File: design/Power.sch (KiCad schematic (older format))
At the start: 62 parts, among them U2 DRV8302, U3 NCP1117ST33T3G

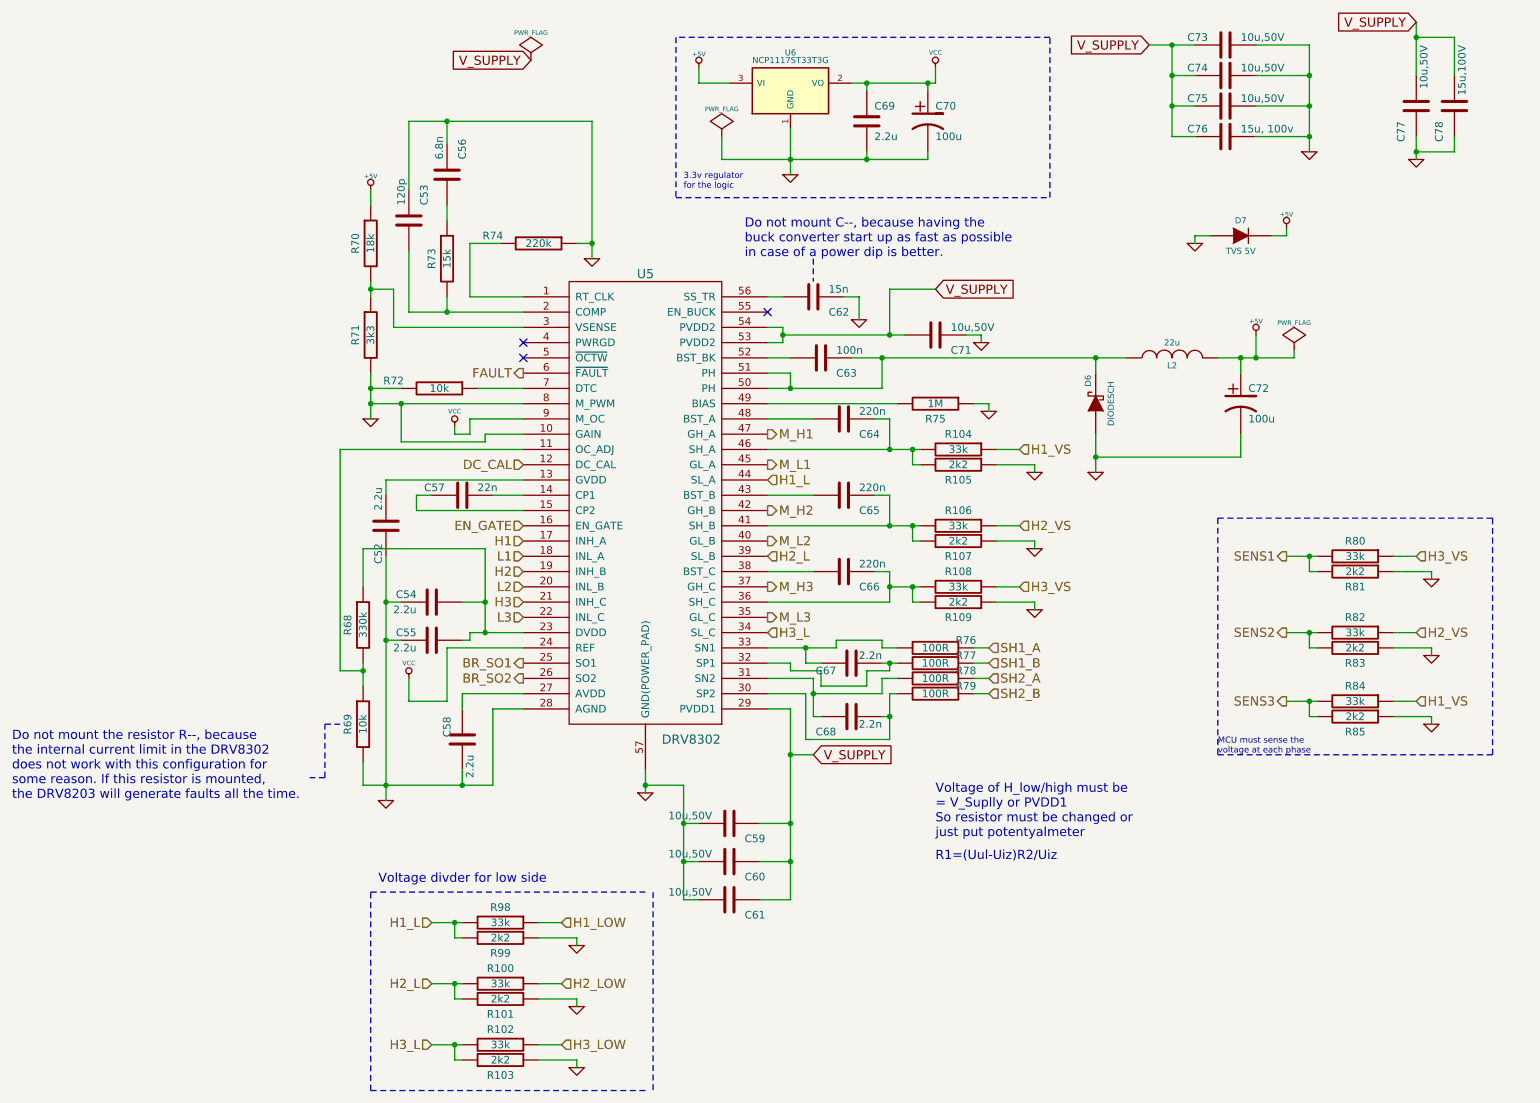
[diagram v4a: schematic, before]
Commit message: Voltage divider for DRV and MCU
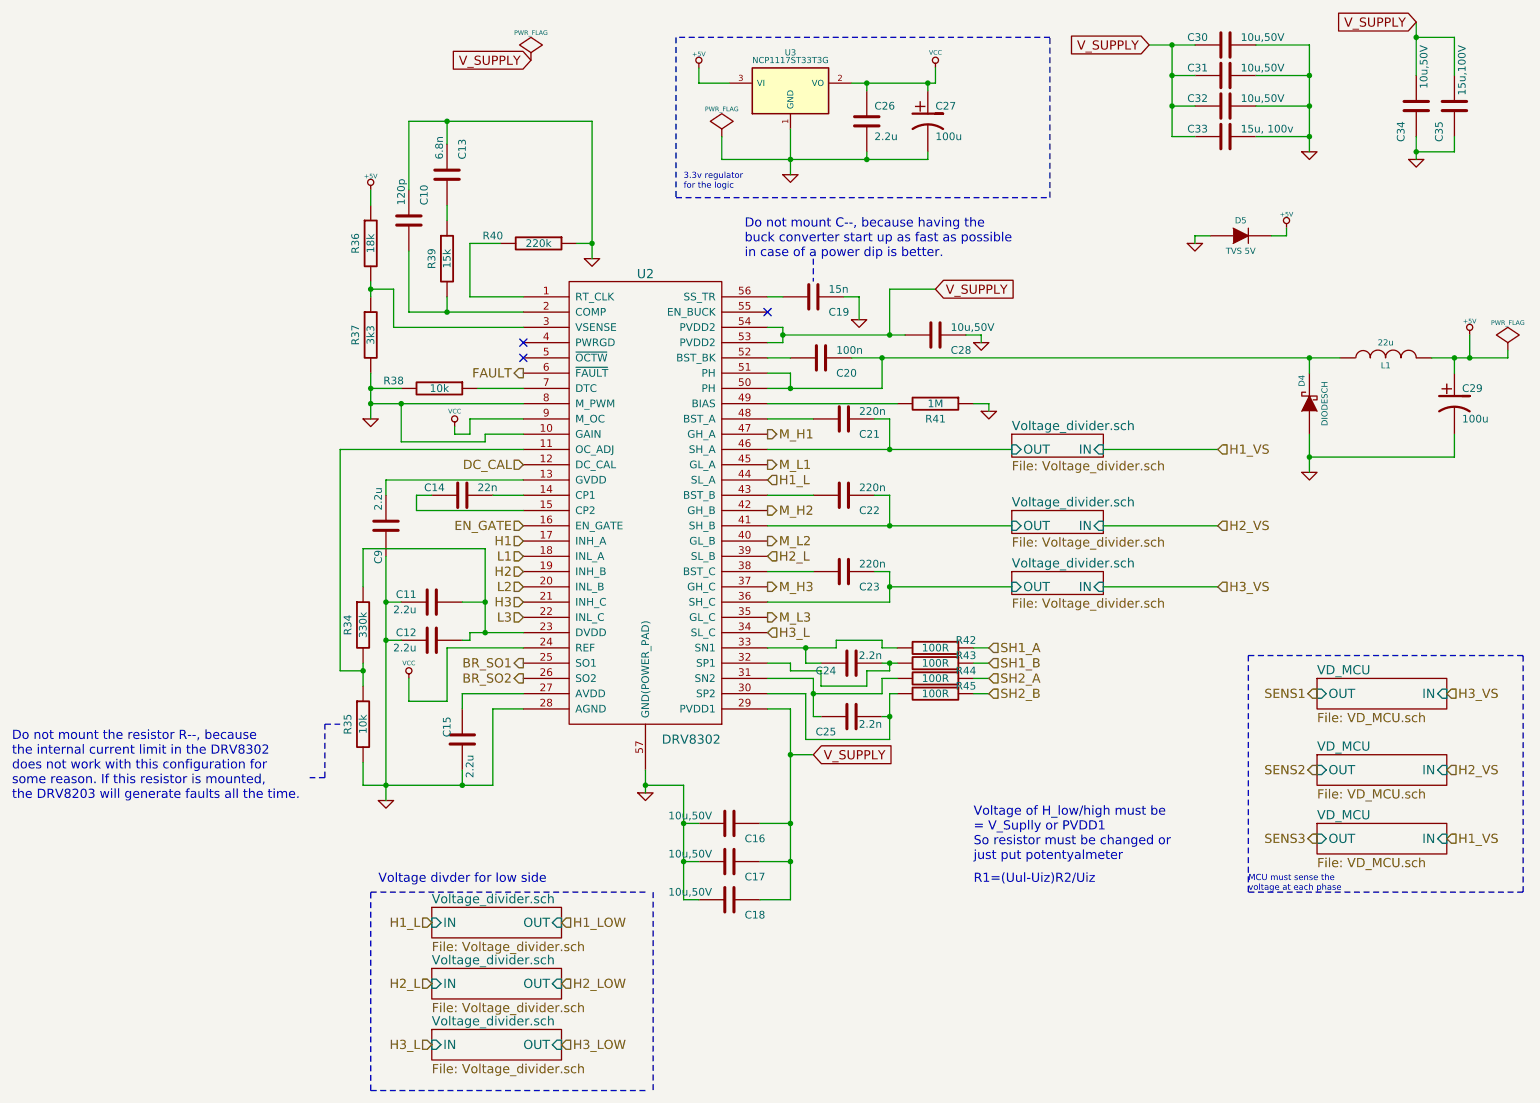
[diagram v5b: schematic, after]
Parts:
- removed R46, R48, R50, R86, R88, R90, R92, R94, R96: 33k, SMD_Packages:SMD-0603_r, symbol R
- removed R47, R49, R51, R87, R89, R91, R93, R95, R97: 2k2, SMD_Packages:SMD-0603_r, symbol R
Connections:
- net Voltage_divider.sch/OUT: now reaches C21.1, U2.46 (SH_A)
- net Voltage_divider.sch/OUT: now reaches C23.1, U2.36 (SH_C)
- net Voltage_divider.sch/OUT: now reaches C22.1, U2.41 (SH_B)
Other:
- moved on the sheet: C29, D4, L1

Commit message: Fix some ERC error, add decoupling cap to Vref+ and make some small changes to lib
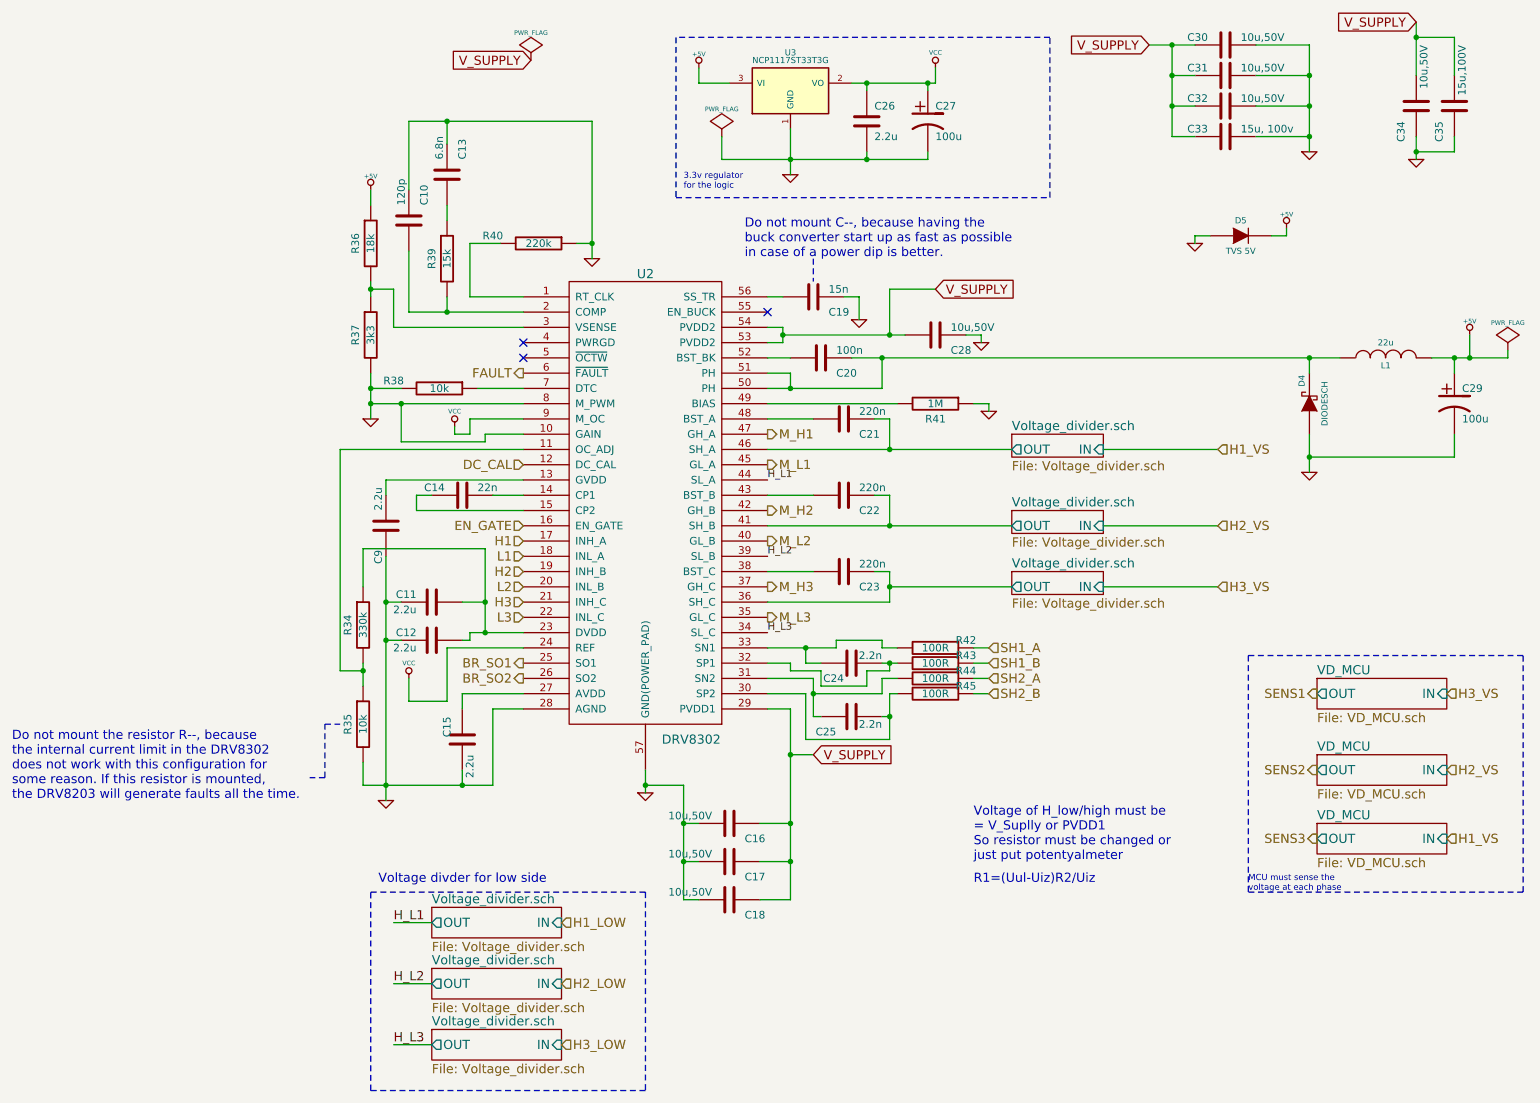
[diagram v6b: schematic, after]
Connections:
- net Voltage_divider.sch/OUT is gone; now on net Voltage_divider.sch/OUT: C22.1, U2.41 (SH_B)
- net Voltage_divider.sch/OUT: no longer C21.1, U2.46 (SH_A)
- net H1_L renamed H_L1
- net H2_L renamed H_L2
- net H3_L renamed H_L3
- new net Voltage_divider.sch/OUT: C21.1, U2.46 (SH_A)

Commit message: PCB
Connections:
- net Voltage_divider.sch/OUT is gone; now on net Voltage_divider.sch/OUT: C22.1, U2.41 (SH_B)
- net Voltage_divider.sch/OUT: no longer C21.1, U2.46 (SH_A)
- new net Voltage_divider.sch/OUT: C21.1, U2.46 (SH_A)
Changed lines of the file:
@@
 AR Path="/504F83BE/504FB755" Ref="#PWR043"  Part="1"
 AR Path="/54B735D5/504FB755" Ref="#PWR079"  Part="1"
-F 0 "#PWR079" H 6750 2700 30  0001 C CNN
+F 0 "#PWR043" H 6750 2700 30  0001 C CNN
 F 1 "GND" H 6750 2630 30  0001 C CNN
 F 2 "" H 6750 2700 60  0001 C CNN
@@
 AR Path="/504F83BE/504FBA7B" Ref="#PWR044"  Part="1"
 AR Path="/54B735D5/504FBA7B" Ref="#PWR080"  Part="1"
-F 0 "#PWR080" H 7600 3300 30  0001 C CNN
+F 0 "#PWR044" H 7600 3300 30  0001 C CNN
 F 1 "GND" H 7600 3230 30  0001 C CNN
 F 2 "" H 7600 3300 60  0001 C CNN
@@
 AR Path="/504F83BE/504FBEC1" Ref="#PWR045"  Part="1"
 AR Path="/54B735D5/504FBEC1" Ref="#PWR081"  Part="1"
-F 0 "#PWR081" H 9700 3700 30  0001 C CNN
+F 0 "#PWR045" H 9700 3700 30  0001 C CNN
 F 1 "GND" H 9700 3630 30  0001 C CNN
 F 2 "" H 9700 3700 60  0001 C CNN
@@
 AR Path="/504F83BE/504FBFA1" Ref="#PWR046"  Part="1"
 AR Path="/54B735D5/504FBFA1" Ref="#PWR082"  Part="1"
-F 0 "#PWR082" H 10750 2890 20  0001 C CNN
+F 0 "#PWR046" H 10750 2890 20  0001 C CNN
 F 1 "+5V" H 10750 2890 30  0000 C CNN
 F 2 "" H 10750 2800 60  0001 C CNN
@@
 AR Path="/504F83BE/504FC2A8" Ref="#PWR047"  Part="1"
 AR Path="/54B735D5/504FC2A8" Ref="#PWR083"  Part="1"
-F 0 "#PWR083" H 3650 5850 30  0001 C CNN
+F 0 "#PWR047" H 3650 5850 30  0001 C CNN
 F 1 "GND" H 3650 5780 30  0001 C CNN
 F 2 "" H 3650 5850 60  0001 C CNN
@@
 AR Path="/504F83BE/504FC918" Ref="#PWR048"  Part="1"
 AR Path="/54B735D5/504FC918" Ref="#PWR084"  Part="1"
-F 0 "#PWR084" H 5350 5800 30  0001 C CNN
+F 0 "#PWR048" H 5350 5800 30  0001 C CNN
 F 1 "GND" H 5350 5730 30  0001 C CNN
 F 2 "" H 5350 5800 60  0001 C CNN
@@
 AR Path="/504F83BE/504FDE04" Ref="#PWR049"  Part="1"
 AR Path="/54B735D5/504FDE04" Ref="#PWR085"  Part="1"
-F 0 "#PWR085" H 3550 3350 30  0001 C CNN
+F 0 "#PWR049" H 3550 3350 30  0001 C CNN
 F 1 "GND" H 3550 3280 30  0001 C CNN
 F 2 "" H 3550 3350 60  0001 C CNN
@@
 AR Path="/504F83BE/504FE598" Ref="#PWR050"  Part="1"
 AR Path="/54B735D5/504FE598" Ref="#PWR086"  Part="1"
-F 0 "#PWR086" H 5000 2300 30  0001 C CNN
+F 0 "#PWR050" H 5000 2300 30  0001 C CNN
 F 1 "GND" H 5000 2230 30  0001 C CNN
 F 2 "" H 5000 2300 60  0001 C CNN
@@
 AR Path="/504F83BE/504FE8CD" Ref="#PWR051"  Part="1"
 AR Path="/54B735D5/504FE8CD" Ref="#PWR087"  Part="1"
-F 0 "#PWR087" H 3550 1940 20  0001 C CNN
+F 0 "#PWR051" H 3550 1940 20  0001 C CNN
 F 1 "+5V" H 3550 1940 30  0000 C CNN
 F 2 "" H 3550 1850 60  0001 C CNN
@@
 AR Path="/504F83BE/50500B40" Ref="#PWR052"  Part="1"
 AR Path="/54B735D5/50500B40" Ref="#PWR088"  Part="1"
-F 0 "#PWR088" H 6300 1750 30  0001 C CNN
+F 0 "#PWR052" H 6300 1750 30  0001 C CNN
 F 1 "GND" H 6300 1680 30  0001 C CNN
 F 2 "" H 6300 1750 60  0001 C CNN
@@
 AR Path="/504F83BE/50500B46" Ref="#PWR053"  Part="1"
 AR Path="/54B735D5/50500B46" Ref="#PWR089"  Part="1"
-F 0 "#PWR089" H 7250 1150 30  0001 C CNN
+F 0 "#PWR053" H 7250 1150 30  0001 C CNN
 F 1 "VCC" H 7250 1150 30  0000 C CNN
 F 2 "" H 7250 1050 60  0001 C CNN
@@
 AR Path="/504F83BE/50500BBC" Ref="#PWR054"  Part="1"
 AR Path="/54B735D5/50500BBC" Ref="#PWR090"  Part="1"
-F 0 "#PWR090" H 5700 1140 20  0001 C CNN
+F 0 "#PWR054" H 5700 1140 20  0001 C CNN
 F 1 "+5V" H 5700 1140 30  0000 C CNN
 F 2 "" H 5700 1050 60  0001 C CNN
@@
 AR Path="/504F83BE/505014BC" Ref="#PWR055"  Part="1"
 AR Path="/54B735D5/505014BC" Ref="#PWR091"  Part="1"
-F 0 "#PWR091" H 3800 5150 30  0001 C CNN
+F 0 "#PWR055" H 3800 5150 30  0001 C CNN
 F 1 "VCC" H 3800 5150 30  0000 C CNN
 F 2 "" H 3800 5050 60  0001 C CNN
@@
 AR Path="/504F83BE/50510100" Ref="#FLG056"  Part="1"
 AR Path="/54B735D5/50510100" Ref="#FLG092"  Part="1"
-F 0 "#FLG092" H 11000 2995 30  0001 C CNN
+F 0 "#FLG056" H 11000 2995 30  0001 C CNN
 F 1 "PWR_FLAG" H 11000 3080 30  0000 C CNN
 F 2 "" H 11000 2900 60  0001 C CNN
@@
 AR Path="/504F83BE/505104A0" Ref="#FLG057"  Part="1"
 AR Path="/54B735D5/505104A0" Ref="#FLG093"  Part="1"
-F 0 "#FLG093" H 5850 1595 30  0001 C CNN
+F 0 "#FLG057" H 5850 1595 30  0001 C CNN
 F 1 "PWR_FLAG" H 5850 1680 30  0000 C CNN
 F 2 "" H 5850 1500 60  0001 C CNN
@@
 AR Path="/504F83BE/505105A5" Ref="#FLG058"  Part="1"
 AR Path="/54B735D5/505105A5" Ref="#FLG094"  Part="1"
-F 0 "#FLG094" H 4600 1095 30  0001 C CNN
+F 0 "#FLG058" H 4600 1095 30  0001 C CNN
 F 1 "PWR_FLAG" H 4600 1180 30  0000 C CNN
 F 2 "" H 4600 1000 60  0001 C CNN
@@
 AR Path="/504F83BE/5051337C" Ref="#PWR059"  Part="1"
 AR Path="/54B735D5/5051337C" Ref="#PWR095"  Part="1"
-F 0 "#PWR095" H 7550 2850 30  0001 C CNN
+F 0 "#PWR059" H 7550 2850 30  0001 C CNN
 F 1 "GND" H 7550 2780 30  0001 C CNN
 F 2 "" H 7550 2850 60  0001 C CNN
@@
 AR Path="/504F83BE/5058357A" Ref="#PWR060"  Part="1"
 AR Path="/54B735D5/5058357A" Ref="#PWR096"  Part="1"
-F 0 "#PWR096" H 4100 3500 30  0001 C CNN
+F 0 "#PWR060" H 4100 3500 30  0001 C CNN
 F 1 "VCC" H 4100 3500 30  0000 C CNN
 F 2 "" H 4100 3400 60  0001 C CNN
@@
 AR Path="/504F83BE/510944D0" Ref="#PWR061"  Part="1"
 AR Path="/54B735D5/510944D0" Ref="#PWR097"  Part="1"
-F 0 "#PWR097" H 9700 1600 30  0001 C CNN
+F 0 "#PWR061" H 9700 1600 30  0001 C CNN
 F 1 "GND" H 9700 1530 30  0001 C CNN
 F 2 "" H 9700 1600 60  0001 C CNN
@@
 0D 0D 85 50 5B 08 A1 71 E3 C6 45 47 47 77 AB F8 CD C0 F0 65 C3 18 9A 0F 4F 4B 4B 4B 51 51 51 53
 53 93 40 20 30 31 31 61 94 40 19 18 18 43 C3 C0 C0 A0 72 FE 07 CF 64 8C 61 E1 12 74 DD 00 00 00
-00 49 45 4E 44 AE 42 60 82 14
+00 49 45 4E 44 AE 42 60 82 D9
 EndData
 $EndBitmap
@@
 20 10 88 31 C3 77 F3 62 81 40 20 10 08 04 02 81 E0 1F 14 E4 21 10 08 04 02 81 40 8C 41 50 90 87
 40 20 10 08 04 02 31 06 41 41 1E 02 81 40 20 10 08 C4 18 E4 FF 01 14 B1 03 90 4A B9 68 69 00 00
-00 00 49 45 4E 44 AE 42 60 82 83
+00 00 49 45 4E 44 AE 42 60 82 21
 EndData
 $EndBitmap
@@
 A1 C7 18 00 00 C0 28 C8 B2 00 00 00 46 41 96 05 00 00 30 0A B2 2C 00 00 80 51 90 65 01 00 00 8C
 82 2C 0B 00 00 60 14 64 59 00 00 00 A3 FC 7F BD 9B 69 A6 C1 67 F0 EA 00 00 00 00 49 45 4E 44 AE
-42 60 82 0B
+42 60 82 09
 EndData
 $EndBitmap
@@
 AB D8 39 0B 59 91 9E DF A8 2A 5B EE 54 3A FD 71 ED 71 2F 29 C3 82 EC 80 87 06 6E C3 98 10 30 3B
 62 9A BB 2D 03 B8 C4 64 FC B5 26 AC 13 9B D1 39 40 41 C1 D6 78 4C 84 BF 94 F0 6F E1 BF 96 F0 0F
-FF 77 E2 FF 1F 0F 43 55 32 21 1C 08 16 00 00 00 00 49 45 4E 44 AE 42 60 82 7C
+FF 77 E2 FF 1F 0F 43 55 32 21 1C 08 16 00 00 00 00 49 45 4E 44 AE 42 60 82 54
 EndData
 $EndBitmap
@@
 AR Path="/504F83BE/548EDECA" Ref="#PWR062"  Part="1"
 AR Path="/54B735D5/548EDECA" Ref="#PWR098"  Part="1"
-F 0 "#PWR098" H 9550 2190 20  0001 C CNN
+F 0 "#PWR062" H 9550 2190 20  0001 C CNN
 F 1 "+5V" H 9550 2190 30  0000 C CNN
 F 2 "" H 9550 2100 60  0001 C CNN
@@
 AR Path="/504F83BE/548EDF07" Ref="#PWR063"  Part="1"
 AR Path="/54B735D5/548EDF07" Ref="#PWR099"  Part="1"
-F 0 "#PWR099" H 8950 2200 30  0001 C CNN
+F 0 "#PWR063" H 8950 2200 30  0001 C CNN
 F 1 "GND" H 8950 2130 30  0001 C CNN
 F 2 "" H 8950 2200 60  0001 C CNN
@@
 AR Path="/504F83BE/548F3DC0" Ref="#PWR064"  Part="1"
 AR Path="/54B735D5/548F3DC0" Ref="#PWR0100"  Part="1"
-F 0 "#PWR0100" H 10400 1650 30  0001 C CNN
+F 0 "#PWR064" H 10400 1650 30  0001 C CNN
 F 1 "GND" H 10400 1580 30  0001 C CNN
 F 2 "" H 10400 1650 60  0001 C CNN
@@
 AB D8 39 0B 59 91 9E DF A8 2A 5B EE 54 3A FD 71 ED 71 2F 29 C3 82 EC 80 87 06 6E C3 98 10 30 3B
 62 9A BB 2D 03 B8 C4 64 FC B5 26 AC 13 9B D1 39 40 41 C1 D6 78 4C 84 BF 94 F0 6F E1 BF 96 F0 0F
-FF 77 E2 FF 1F 0F 43 55 32 21 1C 08 16 00 00 00 00 49 45 4E 44 AE 42 60 82 7C
+FF 77 E2 FF 1F 0F 43 55 32 21 1C 08 16 00 00 00 00 49 45 4E 44 AE 42 60 82 54
 EndData
 $EndBitmap
@@
 AB D8 39 0B 59 91 9E DF A8 2A 5B EE 54 3A FD 71 ED 71 2F 29 C3 82 EC 80 87 06 6E C3 98 10 30 3B
 62 9A BB 2D 03 B8 C4 64 FC B5 26 AC 13 9B D1 39 40 41 C1 D6 78 4C 84 BF 94 F0 6F E1 BF 96 F0 0F
-FF 77 E2 FF 1F 0F 43 55 32 21 1C 08 16 00 00 00 00 49 45 4E 44 AE 42 60 82 7C
+FF 77 E2 FF 1F 0F 43 55 32 21 1C 08 16 00 00 00 00 49 45 4E 44 AE 42 60 82 54
 EndData
 $EndBitmap
